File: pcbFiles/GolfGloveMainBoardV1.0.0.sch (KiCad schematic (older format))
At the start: 35 parts, among them J1 USB_C_Receptacle, J10 A-1JB, J11 Conn_01x16_Male, J12 HOST_WAKE, J13 TP4, J2 Conn_01x06, J3 USB_C_Receptacle, J4 Conn_01x01, J5 Conn_01x01, SW1 SW_SPDT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

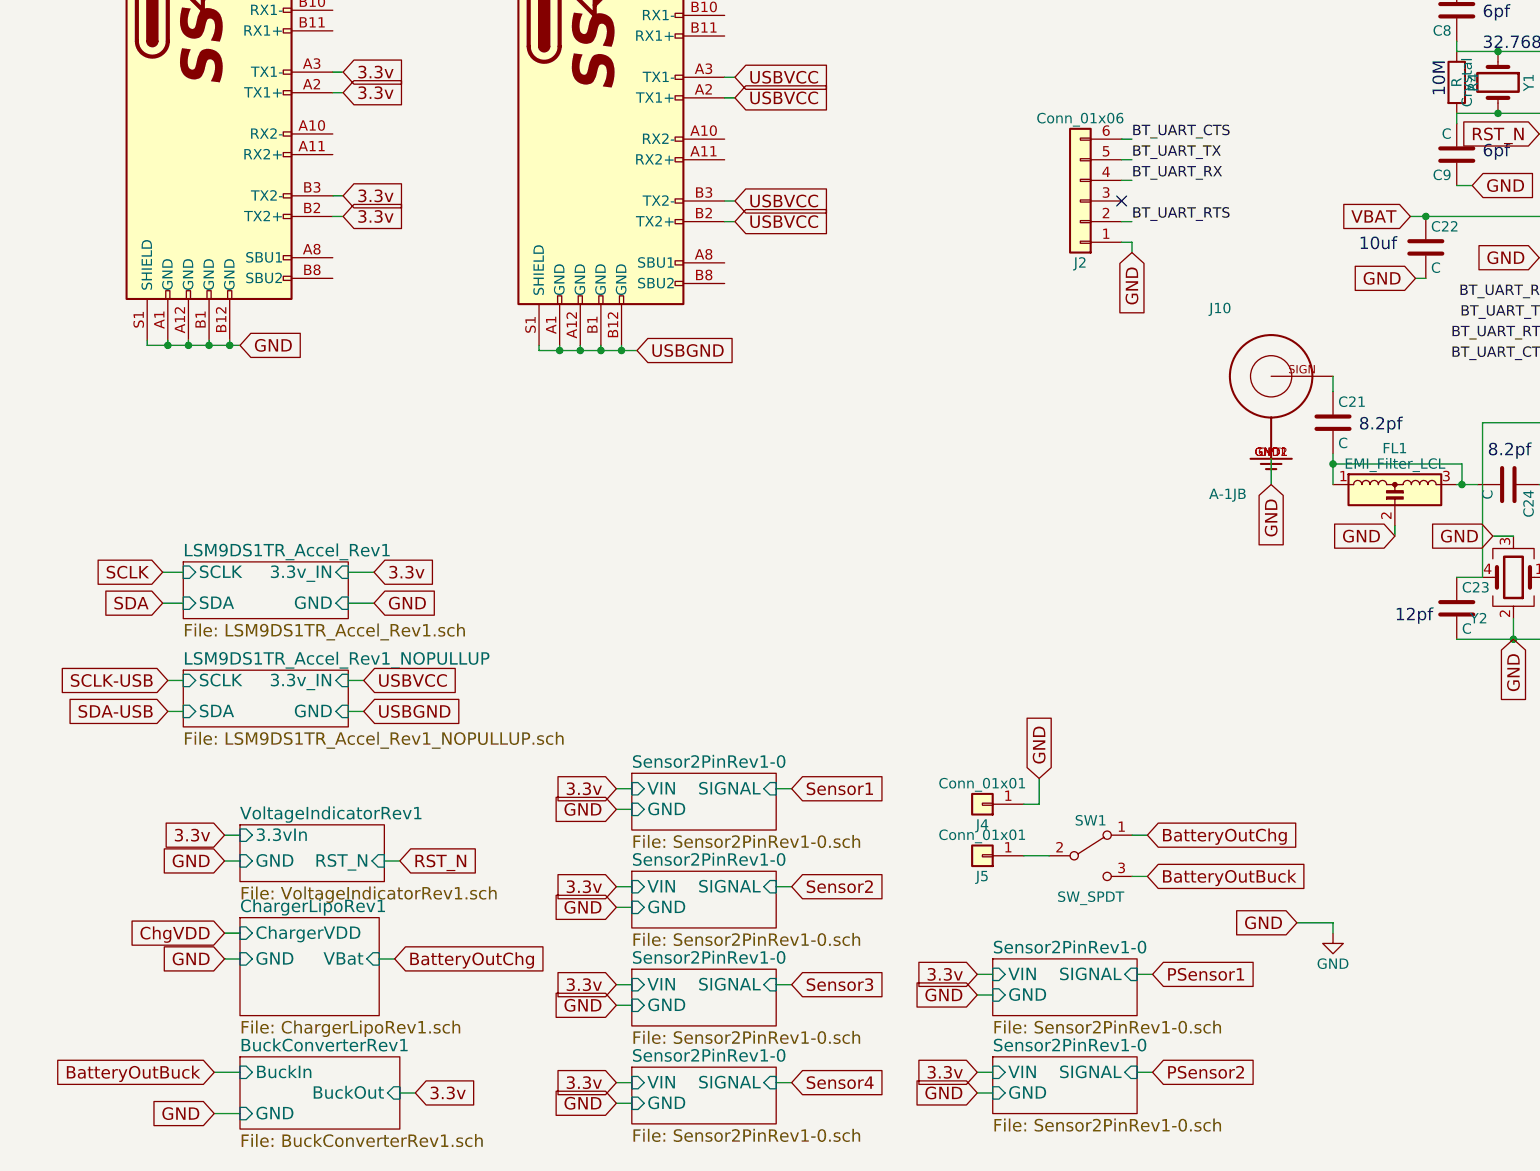
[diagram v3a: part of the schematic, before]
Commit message: Add Pin Header For 5v UART Connection
Added a 1x2 2.54mm Pitch pin header for the 5v UART line. This line feeds directly into the pin of the buck converter and therefore we will need to be sure to NOT turn on the device when programming or when this jumper is connected. @willcarroll7
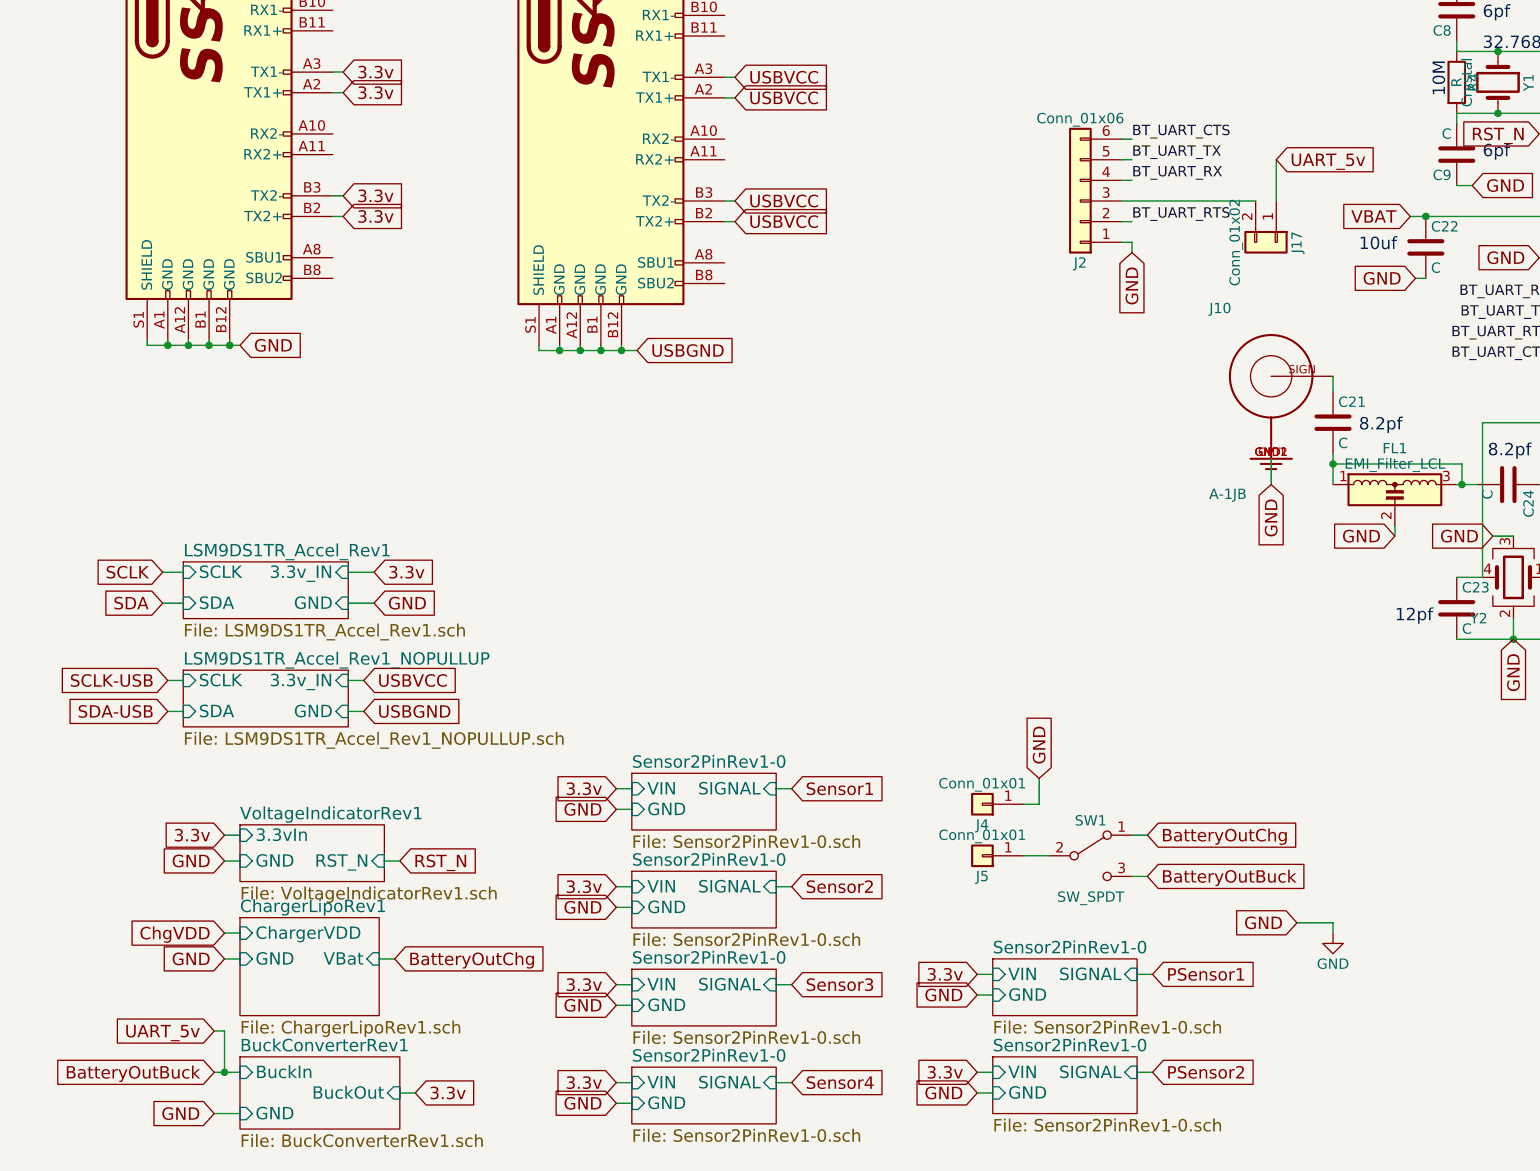
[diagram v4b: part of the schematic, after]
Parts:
- added J17: Conn_01x02, Pin_Headers:Pin_Header_Angled_1x02_Pitch2.54mm, symbol Conn_01x02
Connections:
- net BatteryOutBuck: now also J17.1 (Pin_1)
- net at J2.3 (Pin_3): now also J17.2 (Pin_2)
- no-connect marks 1 -> 0
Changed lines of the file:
@@
 LIBS:contrib
 LIBS:valves
-LIBS:ADS1115IDGST
-LIBS:CYW20719B1KUMLG
-LIBS:LSM9DS1TR
-LIBS:TPS63001DRCT
-LIBS:MCP73831T-2ACI_OT
-LIBS:A-1JB
-LIBS:XC6119N16A7R-G
 LIBS:GolfGloveMainBoardV1.0.0-cache
 EELAYER 25 0
@@
 Wire Wire Line
 	5750 3250 5800 3250
-NoConn ~ 5750 3150
 $Comp
 L Conn_01x06 J2
@@
 GND
 $Comp
-L GND #PWR?
+L GND #PWR1
 U 1 1 5C59B296
 P 6775 6700
-F 0 "#PWR?" H 6775 6450 50  0001 C CNN
+F 0 "#PWR1" H 6775 6450 50  0001 C CNN
 F 1 "GND" H 6775 6550 50  0000 C CNN
 F 2 "" H 6775 6700 50  0001 C CNN
@@
 Wire Wire Line
 	6775 6650 6775 6700
+$Comp
+L Conn_01x02 J17
+U 1 1 5C59DA7F
+P 6500 3350
+F 0 "J17" H 6500 3450 50  0000 C CNN
+F 1 "Conn_01x02" H 6500 3150 50  0000 C CNN
+F 2 "Pin_Headers:Pin_Header_Angled_1x02_Pitch2.54mm" H 6500 3350 50  0001 C CNN
+F 3 "" H 6500 3350 50  0001 C CNN
+	1    6500 3350
+	0    1    1    0
+$EndComp
+Wire Wire Line
+	5750 3150 6400 3150
+Text GLabel 6500 2950 2    60   Input ~ 0
+UART_5v
+Wire Wire Line
+	6500 3150 6500 2950
+Wire Wire Line
+	1400 7375 1400 7175
+Wire Wire Line
+	1400 7175 1350 7175
+Connection ~ 1400 7375
+Text GLabel 1350 7175 0    60   Input ~ 0
+UART_5v
 $EndSCHEMATC

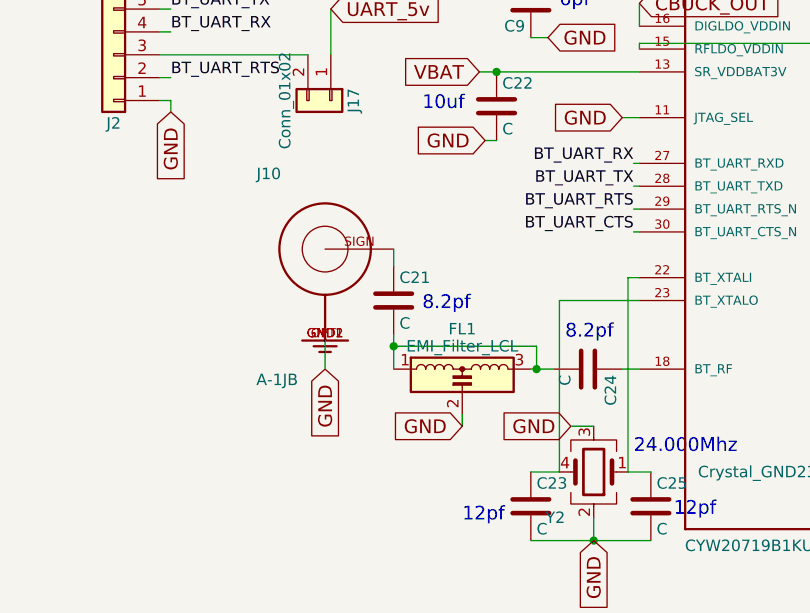
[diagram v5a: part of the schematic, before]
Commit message: Remove Antenna
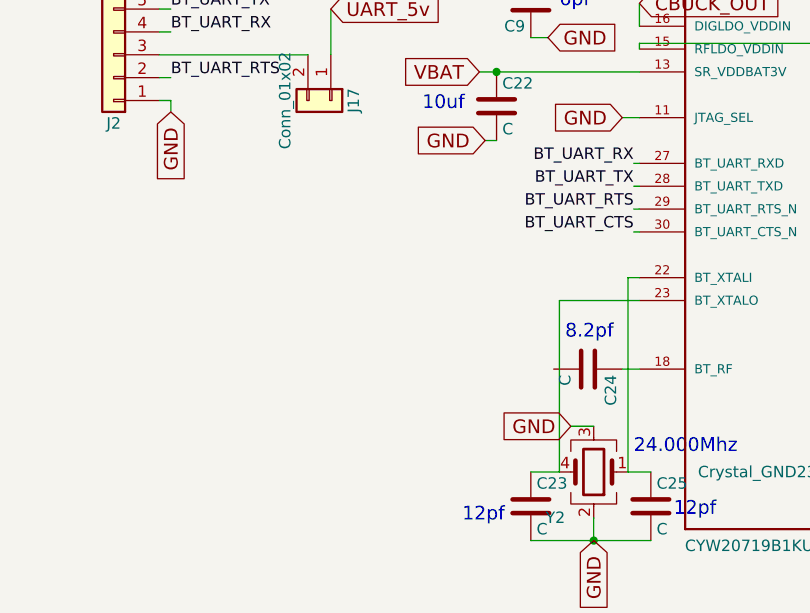
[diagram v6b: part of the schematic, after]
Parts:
- removed C21: C, Capacitors_SMD:C_0402, symbol C
- removed FL1: EMI_Filter_LCL, Resistors_SMD:R_0603, symbol EMI_Filter_LCL
- removed J10: A-1JB, A-1JB:AMPHENOL_A-1JB, symbol A-1JB
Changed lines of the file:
@@
 	9475 4625 9925 4625
-$Comp
-L EMI_Filter_LCL FL1
-U 1 1 5C45A66F
-P 7075 4625
-F 0 "FL1" H 7075 4900 50  0000 C CNN
-F 1 "EMI_Filter_LCL" H 7075 4825 50  0000 C CNN
-F 2 "Resistors_SMD:R_0603" V 7075 4625 50  0001 C CNN
-F 3 "" V 7075 4625 50  0001 C CNN
-	1    7075 4625
-	1    0    0    -1
-$EndComp
-$Comp
-L C C21
-U 1 1 5C45A88F
-P 6775 4225
-F 0 "C21" H 6800 4325 50  0000 L CNN
-F 1 "C" H 6800 4125 50  0000 L CNN
-F 2 "Capacitors_SMD:C_0402" H 6813 4075 50  0001 C CNN
-F 3 "" H 6775 4225 50  0001 C CNN
-	1    6775 4225
-	1    0    0    -1
-$EndComp
-Wire Wire Line
-	6775 4375 6775 4525
-Text GLabel 7075 4775 0    60   Input ~ 0
-GND
-$Comp
-L A-1JB J10
-U 1 1 5C45ABF7
-P 6475 4000
-F 0 "J10" H 6175 4300 50  0000 L BNN
-F 1 "A-1JB" H 6174 3399 50  0000 L BNN
-F 2 "A-1JB:AMPHENOL_A-1JB" H 6475 4000 50  0001 L BNN
-F 3 "None" H 6475 4000 50  0001 L BNN
-F 4 "Amphenol RF" H 6475 4000 50  0001 L BNN "Field4"
-F 5 "None" H 6475 4000 50  0001 L BNN "Field5"
-F 6 "Unavailable" H 6475 4000 50  0001 L BNN "Field6"
-F 7 "Connector; RF; AMC; PCB Jack; Surface Mnt; 50 Ohm; Solder" H 6475 4000 50  0001 L BNN "Field7"
-F 8 "A-1JB" H 6475 4000 50  0001 L BNN "Field8"
-	1    6475 4000
-	1    0    0    -1
-$EndComp
-Text GLabel 6475 4525 3    60   Input ~ 0
-GND
-Wire Wire Line
-	6475 4400 6475 4525
-Wire Wire Line
-	6775 4000 6775 4075
-Text Notes 6900 4275 0    60   ~ 0
-8.2pf
-Wire Wire Line
-	7075 4725 7075 4775
 $Comp
 L C C24
@@
 	0    1    1    0
 $EndComp
-Wire Wire Line
-	7375 4525 7475 4525
 Wire Wire Line
 	7775 4525 7850 4525
@@
 Wire Wire Line
 	3875 2650 3825 2650
-Wire Wire Line
-	6775 4425 7400 4425
-Wire Wire Line
-	7400 4425 7400 4525
-Connection ~ 7400 4525
-Connection ~ 6775 4425
 $Sheet
 S 1475 7300 775  350

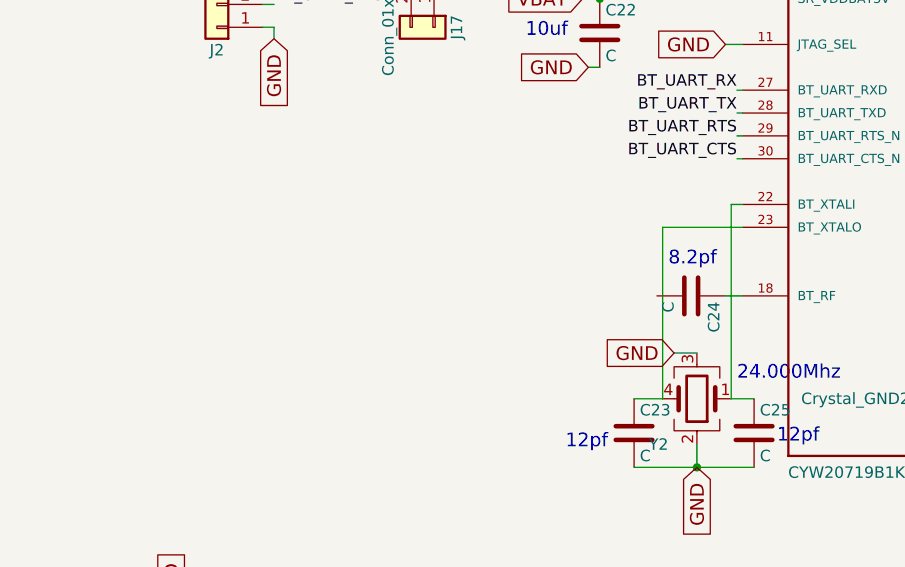
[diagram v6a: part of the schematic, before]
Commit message: Add Antenna And Inductors
Added Inductors and Antenna to the schematic based on the 2450AT42B100E Datasheet. @willcarroll7
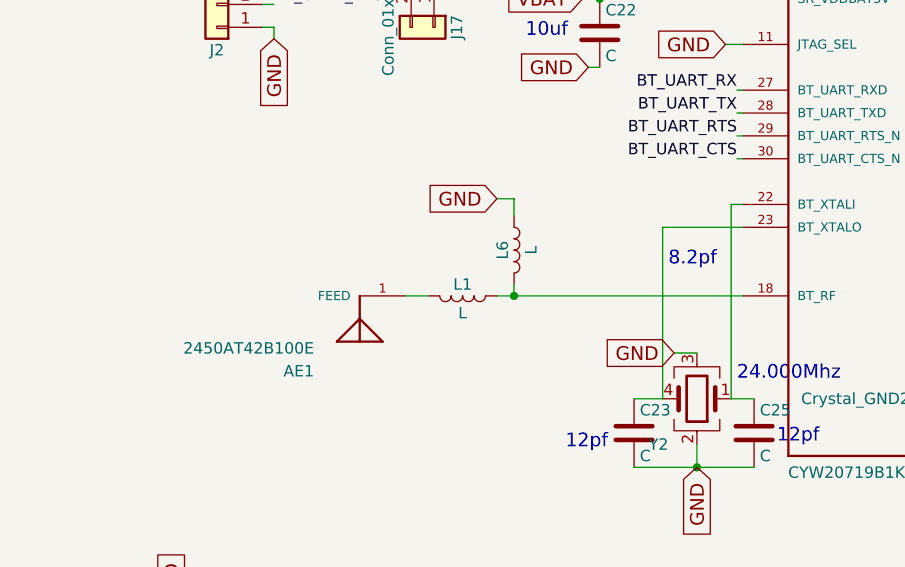
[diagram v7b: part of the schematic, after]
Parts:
- removed C24: C, Capacitors_SMD:C_0402, symbol C
- added AE1: 2450AT42B100E, ANTENNA---------------------:XCVR_2450AT42B100E, symbol 2450AT42B100E
- added L1, L6: L, Inductors_SMD:L_0402, symbol L
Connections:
- net GND: now also L6.1
- net at U4.18 (BT_RF): now also L1.1, L6.2
- new net: AE1.1 (FEED), L1.2
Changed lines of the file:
@@
 LIBS:contrib
 LIBS:valves
+LIBS:2450AT42B100E
 LIBS:GolfGloveMainBoardV1.0.0-cache
 EELAYER 25 0
@@
 Wire Wire Line
 	9475 4625 9925 4625
-$Comp
-L C C24
-U 1 1 5C45B773
-P 7625 4525
-F 0 "C24" H 7650 4625 50  0000 L CNN
-F 1 "C" H 7650 4425 50  0000 L CNN
-F 2 "Capacitors_SMD:C_0402" H 7663 4375 50  0001 C CNN
-F 3 "" H 7625 4525 50  0001 C CNN
-	1    7625 4525
-	0    1    1    0
-$EndComp
-Wire Wire Line
-	7775 4525 7850 4525
+Wire Wire Line
+	6775 4525 7850 4525
 Text Notes 7525 4400 0    60   ~ 0
 8.2pf
@@
 GND
 $Comp
-L GND #PWR01
+L GND #PWR1
 U 1 1 5C59B296
 P 6775 6700
-F 0 "#PWR01" H 6775 6450 50  0001 C CNN
+F 0 "#PWR1" H 6775 6450 50  0001 C CNN
 F 1 "GND" H 6775 6550 50  0000 C CNN
 F 2 "" H 6775 6700 50  0001 C CNN
@@
 Text GLabel 1350 7175 0    60   Input ~ 0
 UART_5v
+$Comp
+L 2450AT42B100E AE1
+U 1 1 5C59CB0B
+P 6175 4525
+F 0 "AE1" H 6375 4825 50  0000 L BNN
+F 1 "2450AT42B100E" H 6375 4725 50  0000 L BNN
+F 2 "ANTENNA---------------------:XCVR_2450AT42B100E" H 6175 4525 50  0001 L BNN
+F 3 "None" H 6175 4525 50  0001 L BNN
+F 4 "Unavailable" H 6175 4525 50  0001 L BNN "Field4"
+F 5 "2450AT42B100E" H 6175 4525 50  0001 L BNN "Field5"
+F 6 "Johanson Technology" H 6175 4525 50  0001 L BNN "Field6"
+F 7 "Antenna Chip 2.4ghz" H 6175 4525 50  0001 L BNN "Field7"
+F 8 "None" H 6175 4525 50  0001 L BNN "Field8"
+	1    6175 4525
+	-1   0    0    1
+$EndComp
+$Comp
+L L L1
+U 1 1 5C59D98B
+P 6625 4525
+F 0 "L1" V 6575 4525 50  0000 C CNN
+F 1 "L" V 6700 4525 50  0000 C CNN
+F 2 "Inductors_SMD:L_0402" H 6625 4525 50  0001 C CNN
+F 3 "" H 6625 4525 50  0001 C CNN
+	1    6625 4525
+	0    1    1    0
+$EndComp
+$Comp
+L L L6
+U 1 1 5C59DAC4
+P 6850 4325
+F 0 "L6" V 6800 4325 50  0000 C CNN
+F 1 "L" V 6925 4325 50  0000 C CNN
+F 2 "Inductors_SMD:L_0402" H 6850 4325 50  0001 C CNN
+F 3 "" H 6850 4325 50  0001 C CNN
+	1    6850 4325
+	1    0    0    -1
+$EndComp
+Text GLabel 6775 4100 0    60   Input ~ 0
+GND
+Wire Wire Line
+	6775 4100 6850 4100
+Wire Wire Line
+	6850 4100 6850 4175
+Wire Wire Line
+	6850 4525 6850 4475
+Connection ~ 6850 4525
+Wire Wire Line
+	6375 4525 6475 4525
 $EndSCHEMATC

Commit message: Update Circuit With Antenna
This commit will update the pcb with a mock up of the antenna design without the vias, this commit will also update the pressure sensors to be attached to the top of hand unit to allow for USB-C Connection. @willcarroll7
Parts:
- J17: footprint Pin_Headers:Pin_Header_Angled_1x02_Pitch2.54mm -> Pin_Headers:Pin_Header_Straight_1x02_Pitch2.54mm
- L2: footprint Inductors_SMD:L_0805 -> Inductors_SMD:L_0402
- SW1: footprint SDPT:SDTPSwitchAmazon -> Buttons_Switches_SMD:SW_SPDT_PCM12
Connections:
- net PSensor1: now also J3.A10 (RX2-), J3.B10 (RX1-); no longer J11.9 (Pin_9), U4.38 (P17)
- net PSensor2: now also J3.A11 (RX2+), J3.B11 (RX1+); no longer J11.16 (Pin_16), U4.6 (P38)
- new net: J11.9 (Pin_9), U4.38 (P17)
- new net: J11.16 (Pin_16), U4.6 (P38)
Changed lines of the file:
@@
 LIBS:valves
 LIBS:2450AT42B100E
+LIBS:A-1JB
+LIBS:ADS1115IDGST
+LIBS:CD4011BM96
+LIBS:CYW20719B1KUMLG
+LIBS:LSM9DS1TR
+LIBS:MCP73831T-2ACI_OT
+LIBS:MMDT3904V-7
+LIBS:MMPQ3904
+LIBS:S2B-PH-K-S_LF__SN_
+LIBS:TPS63001DRCT
+LIBS:XC6119N16A7R-G
 LIBS:GolfGloveMainBoardV1.0.0-cache
 EELAYER 25 0
@@
 F 0 "SW1" H 5600 6495 50  0000 C CNN
 F 1 "SW_SPDT" H 5600 6125 50  0000 C CNN
-F 2 "SDPT:SDTPSwitchAmazon" H 5600 6325 50  0001 C CNN
+F 2 "Buttons_Switches_SMD:SW_SPDT_PCM12" H 5600 6325 50  0001 C CNN
 F 3 "" H 5600 6325 50  0001 C CNN
 	1    5600 6325
@@
 Text GLabel 5900 6900 2    60   Input ~ 0
 PSensor1
-Text GLabel 10575 4125 2    60   Input ~ 0
+Text GLabel 3900 2350 2    60   Input ~ 0
 PSensor2
-Text GLabel 10575 4000 2    60   Input ~ 0
+Text GLabel 3900 2250 2    60   Input ~ 0
 PSensor1
 Text GLabel 9925 4325 2    60   Input ~ 0
@@
 F 0 "L2" V 10000 3125 50  0000 C CNN
 F 1 "L" V 10125 3125 50  0000 C CNN
-F 2 "Inductors_SMD:L_0805" H 10050 3125 50  0001 C CNN
+F 2 "Inductors_SMD:L_0402" H 10050 3125 50  0001 C CNN
 F 3 "" H 10050 3125 50  0001 C CNN
 	1    10050 3125
@@
 Wire Wire Line
 	9925 3875 10575 3875
-Wire Wire Line
-	10000 4000 10575 4000
-Wire Wire Line
-	10575 4125 10475 4125
-Wire Wire Line
-	10475 4125 10475 4925
-Wire Wire Line
-	10475 4925 9475 4925
 $Comp
 L Conn_01x16_Male J11
@@
 Wire Wire Line
 	9475 4125 9925 4125
-Wire Wire Line
-	9475 4225 10000 4225
 Connection ~ 9850 4325
 Wire Wire Line
@@
 Connection ~ 9850 4525
 Connection ~ 9850 4625
-Connection ~ 9850 4925
 Text GLabel 7775 2825 0    60   Input ~ 0
 RST_N
 Wire Wire Line
 	7775 2825 7850 2825
-Wire Wire Line
-	10000 4225 10000 4000
-Connection ~ 9850 4225
 Wire Wire Line
 	9925 4125 9925 3875
@@
 3.3v
 Text GLabel 5050 7000 0    60   Input ~ 0
-GND
+USBGND
 Text GLabel 5050 6900 0    60   Input ~ 0
-3.3v
+USBVCC
 Text GLabel 5050 7475 0    60   Input ~ 0
-GND
+USBGND
 Text GLabel 5050 7375 0    60   Input ~ 0
-3.3v
+USBVCC
 Wire Wire Line
 	3300 6000 3375 6000
@@
 GND
 $Comp
-L GND #PWR1
+L GND #PWR01
 U 1 1 5C59B296
 P 6775 6700
-F 0 "#PWR1" H 6775 6450 50  0001 C CNN
+F 0 "#PWR01" H 6775 6450 50  0001 C CNN
 F 1 "GND" H 6775 6550 50  0000 C CNN
 F 2 "" H 6775 6700 50  0001 C CNN
@@
 F 0 "J17" H 6500 3450 50  0000 C CNN
 F 1 "Conn_01x02" H 6500 3150 50  0000 C CNN
-F 2 "Pin_Headers:Pin_Header_Angled_1x02_Pitch2.54mm" H 6500 3350 50  0001 C CNN
+F 2 "Pin_Headers:Pin_Header_Straight_1x02_Pitch2.54mm" H 6500 3350 50  0001 C CNN
 F 3 "" H 6500 3350 50  0001 C CNN
 	1    6500 3350
@@
 Wire Wire Line
 	6375 4525 6475 4525
+Wire Wire Line
+	9850 4925 9475 4925
+Wire Wire Line
+	9475 4225 9850 4225
+Text GLabel 3900 2950 2    60   Input ~ 0
+PSensor2
+Text GLabel 3900 2850 2    60   Input ~ 0
+PSensor1
+Wire Wire Line
+	3825 2250 3900 2250
+Wire Wire Line
+	3825 2350 3900 2350
+Wire Wire Line
+	3825 2850 3900 2850
+Wire Wire Line
+	3900 2950 3825 2950
 $EndSCHEMATC
